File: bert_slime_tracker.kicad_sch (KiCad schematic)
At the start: 20 parts, among them CN1 SM05B-SRSS-TB (LF)(SN), SW1 MK-12C02-G020, U1 ICM-45686, U2 QMC6309, Y1 1532H-24.000JWVDTL

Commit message: added schematic files
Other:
- note added: "24 MHz Clock"
- title: (none) -> Bert's SlimeVR Tracker
- moved on the sheet: C1, C2, C3, JP1, R4, R5, U1, U2, Y1

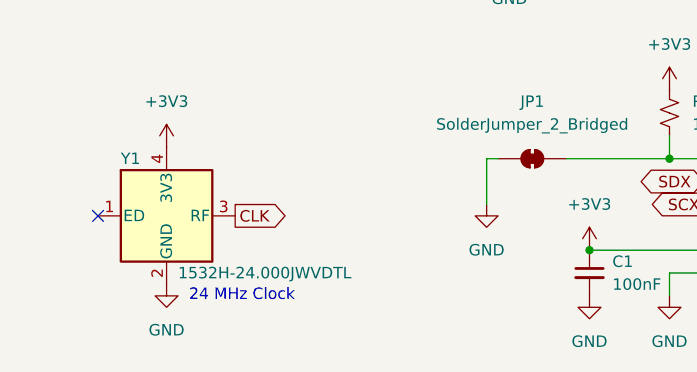
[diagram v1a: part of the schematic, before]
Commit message: updated to corrected oscillator
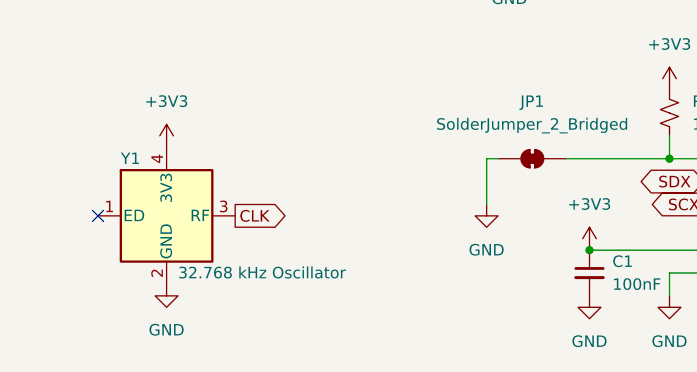
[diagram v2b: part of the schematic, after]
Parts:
- Y1: value 1532H-24.000JWVDTL -> 32.768 kHz Oscillator; symbol Bert-Slime-PCB:1532H-24.000JWVDTL -> Bert-Slime-PCB:O3232768153320JY; LCSC Part C19674145 -> C555607
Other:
- note removed: "24 MHz Clock"
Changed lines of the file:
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@@
 		(title "Bert's SlimeVR Tracker")
 	)
-	(text "24 MHz Clock"
-		(exclude_from_sim no)
-		(at 71.882 151.13 0)
-		(effects
-			(font
-				(size 1.27 1.27)
-			)
-		)
-	)
 	(junction
 		(at 255.27 140.97)
@@
 	)
 	(symbol
-		(lib_id "Bert-Slime-PCB:1532H-24.000JWVDTL")
+		(lib_id "Bert-Slime-PCB:O3232768153320JY")
 		(at 63.5 142.24 0)
 		(unit 1)
@@
 			)
 		)
-		(property "Value" "1532H-24.000JWVDTL"
+		(property "Value" "32.768 kHz Oscillator"
 			(at 64.77 148.59 0)
 			(effects
@@
 			)
 		)
-		(property "Datasheet" "https://jlcpcb.com/api/file/downloadByFileSystemAccessId/8590892673421160448"
+		(property "Datasheet" "https://jlcpcb.com/api/file/downloadByFileSystemAccessId/8590171186467942400"
 			(at 60.96 142.24 0)
 			(effects
@@
 			)
 		)
-		(property "Description" "3.3V ±10ppm ±30ppm HCMOS 8MHz SMD3225-4P Crystal Oscillators"
+		(property "Description" "3.3V 5mA ±20ppm CMOS 32.768kHz SMD3225-4P Crystal Oscillators ROHS"
 			(at 63.5 142.24 0)
 			(effects
@@
 			)
 		)
-		(property "LCSC Part" "C19674145"
+		(property "LCSC Part" "C555607"
 			(at 63.5 142.24 0)
 			(effects
